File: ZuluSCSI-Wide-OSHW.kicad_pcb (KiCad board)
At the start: 4 copper layers, 100 x 93.5 mm, 170 parts, among them J1 USB_DATA, J2 TF003, J3 Conn_01x02, J4 MnL, J5 HD68, J6 Conn_01x05, J7 Conn_01x04, J8 Conn_01x02, Q1 AO3401A, Q10 AO3401A, Q11 AO3401A, Q12 AO3401A, Q13 AO3401A, Q14 AO3401A, Q15 AO3401A, Q16 AO3401A, Q17 AO3401A, Q18 AO3401A, Q19 AO3401A, Q2 AO3401A, Q20 AO3401A, Q21 AO3401A, Q22 AO3401A, Q23 AO3401A, Q24 AO3401A, Q25 AO3401A, Q26 AO3401A, Q27 AO3401A, Q3 AO3401A, Q4 AO3401A, Q5 AO3401A, Q6 AO3401A, Q7 AO3401A, Q8 AO3401A, Q9 AO3401A, SW1 SW_DIP_x03, SW2 SW_EJECT, SW3 SW_BOOT, U1 RP2350_80QFN, U10 W25Q128JVS, U11 74LVT245, U2 74LVT245, U3 74LVT245, U4 74LVT245, U5 74LVT125, U6 74LVT125, U7 AZ1117-2.85, U8 AP62250WU, U9 USB TVS, Y1 12MHz

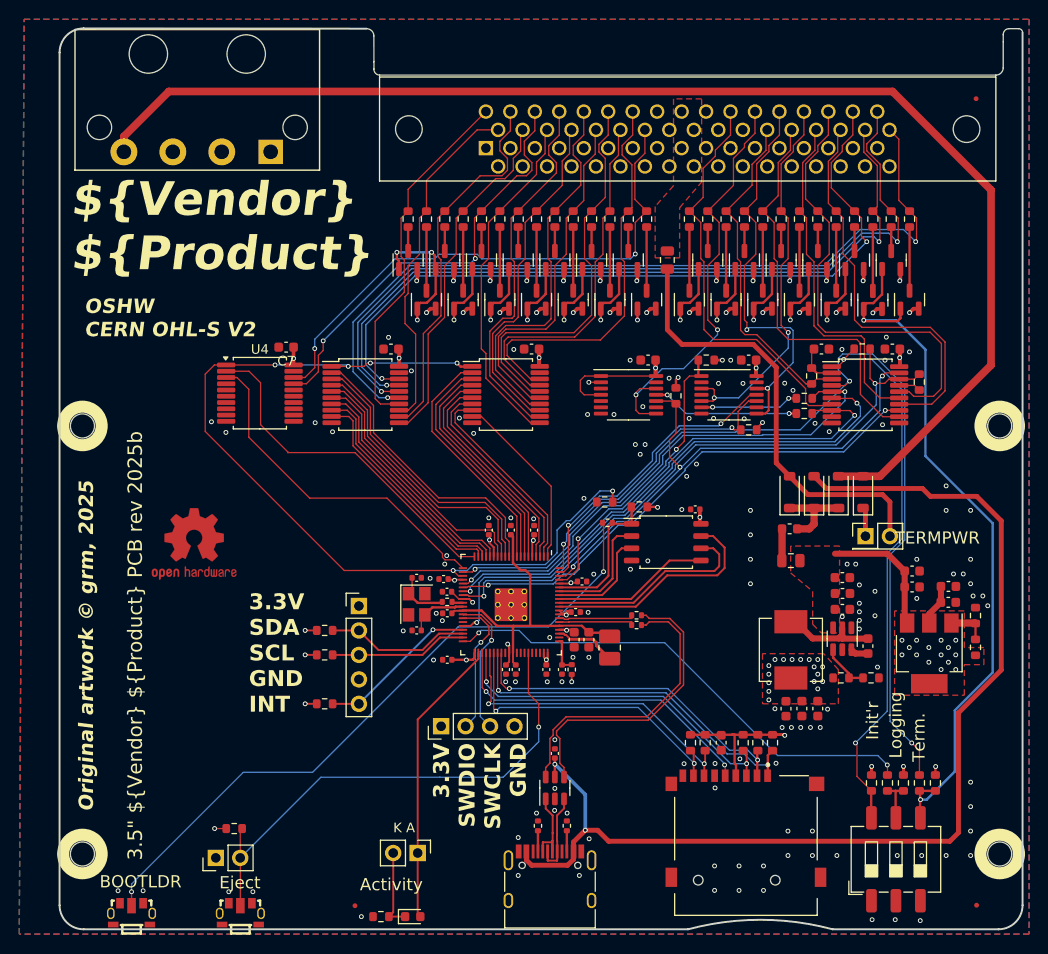
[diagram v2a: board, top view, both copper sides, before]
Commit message: PCB Update, Layout and DRC passed for rev 2026a
Schematic updated with more features from the ZuluSCSI wide board.
JLCPCB parts orientation and position adjusted.
Silkscreen updated

Features added:
- Pico SWD debug header (3 Pin JST header)
- I2C QWIIC header added (4 pin JST header)
- I2S Header added, compatible with AdaFruit PCM510x I2S DACs
- 4 Pin 0.1" (2.54mm) pitch power header added
- Github Workflow for auto generation of Gerbers, BOM, and Pos files
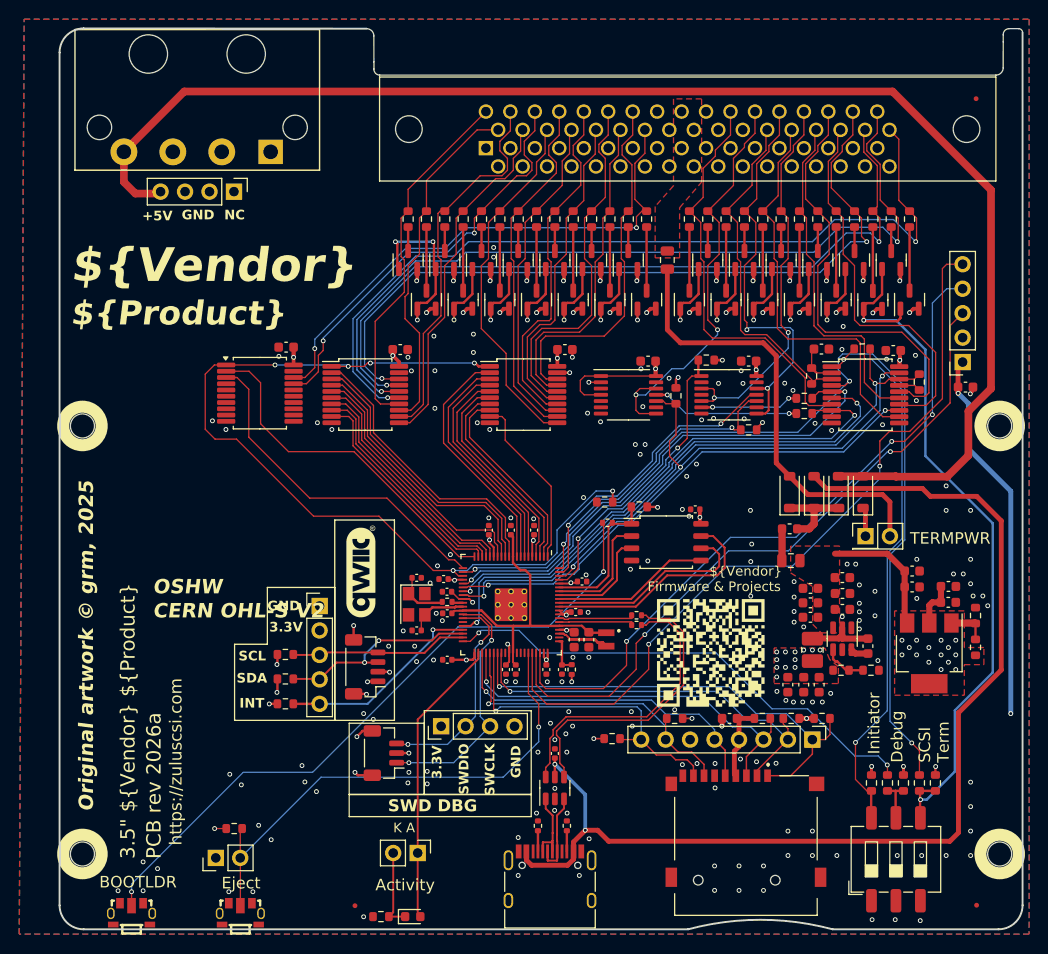
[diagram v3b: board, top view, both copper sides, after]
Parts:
- removed the REF** at (40.8, 96.7)
- added C19: 10uF, Capacitor_SMD:C_0603_1608Metric, F.Cu at (120.9, 80.4)
- added C40: 10uF, Capacitor_SMD:C_0603_1608Metric, F.Cu at (104.8, 101.3)
- added C41: 10uF, Capacitor_SMD:C_0603_1608Metric, F.Cu at (104.8, 104.3)
- added C42: 10uF, Capacitor_SMD:C_0603_1608Metric, F.Cu at (104.8, 102.8)
- added J10: I2S, ZuluSCSI-Wide-OSHW:PCM510x_1x05_P2.54mm_Vertical, F.Cu at (120.6, 77.8)
- added J11: SD_HEADER, Connector_PinHeader_2.54mm:PinHeader_1x08_P2.54mm_Vertical, F.Cu at (105.0, 117.0)
- added J303: QWIIC, Connector_JST:JST_SH_BM04B-SRSS-TB_1x04-1MP_P1.00mm_Vertical, F.Cu at (58.6, 109.4)
- added J311: PICO_DBG, Connector_JST:JST_SH_BM03B-SRSS-TB_1x03-1MP_P1.00mm_Vertical, F.Cu at (60.5, 118.4)
- added J9: PHeader, Connector_PinHeader_2.54mm:PinHeader_1x04_P2.54mm_Vertical, F.Cu at (44.9, 60.1)
- added REF**: OSHW-Logo2_14.6x12mm_Copper, Symbol:OSHW-Logo2_14.6x12mm_Copper, F.Cu at (43.4, 94.1)
- L2: footprint Inductor_SMD:L_Vishay_IHLP-2525 -> Inductor_SMD:L_1008_2520Metric_Pad1.43x2.20mm_HandSolder
- L3: value 3.3uH -> 3.3u; footprint Inductor_SMD:L_1008_2520Metric_Pad1.43x2.20mm_HandSolder -> ZuluSCSI-Wide-OSHW:L_pol_2016
- SW2: value SW_EJECT -> SW_PUSH
- SW3: value SW_BOOT -> SW_PUSH
- moved R7 8.15 mm to (84.2, 116.9), turned to 180 degrees
- moved R1 5.73 mm to (106.0, 114.8), turned to 180 degrees
- moved R51 4.78 mm to (50.3, 110.7)
- moved R15 4.78 mm to (50.3, 108.2)
- moved R2 4.28 mm to (102.8, 114.8), turned to 0 degrees
- moved C16 4.25 mm to (105.7, 111.3)
- moved J6 4.08 mm to (53.8, 103.1)
- moved R52 4.08 mm to (50.3, 113.3)
- moved R5 4.05 mm to (90.7, 114.8), turned to 0 degrees
- moved C4 3.46 mm to (79.3, 76.5), turned to 0 degrees
- moved R3 3.21 mm to (99.8, 114.8), turned to 180 degrees
- moved C12 2.88 mm to (104.1, 111.3)
- moved C13 2.88 mm to (102.4, 111.3)
- moved C1 2.67 mm to (96.4, 114.8), turned to 180 degrees
- moved L2 2.23 mm to (105.0, 107.7)
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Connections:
- J6 pad 1: +3V3 -> GND
- J6 pad 2: /I²C_SDA -> +3V3
- J6 pad 4: GND -> /I²C_SDA
- R15 pad 1: /I²C_SDA -> /I²C_SCL
- R51 pad 1: /I²C_SCL -> /I²C_SDA
- U1 pad 56: unconnected-(U1-GPIO45_ADC5-Pad56) -> /I2S_CK
- U1 pad 57: unconnected-(U1-GPIO46_ADC6-Pad57) -> /I2S_WS
- U1 pad 58: unconnected-(U1-GPIO47_ADC7-Pad58) -> /I2S_SD
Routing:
- net /I2S_CK: track 0.00 -> 79.8 mm, vias 0 -> 2
- net /I2S_SD: track 0.00 -> 72.7 mm, vias 0 -> 3
- net /I2S_WS: track 0.00 -> 70.9 mm, vias 0 -> 2
- net +3V3: track 50.1 -> 86.2 mm
- net GND: track 1.25 -> 14.0 mm, vias 132 -> 185
- net /SWCLK: track 14.9 -> 26.1 mm, vias 1 -> 2
- net /SDIO_D2: track 37.9 -> 49.2 mm, vias 2 -> 1
- net /5V_IN: track 136.6 -> 147.4 mm
- net /SWD: track 14.4 -> 22.4 mm, vias 1 -> 2
- net /SDIO_D3: track 35.6 -> 42.8 mm, vias 2 -> 1
- net /I²C_SDA: track 15.1 -> 21.5 mm, vias 0 -> 2
- net /SDIO_CMD: track 36.5 -> 41.5 mm, vias 2 -> 1
- net /I²C_INT: track 16.7 -> 21.3 mm
- net /I²C_SCL: track 14.3 -> 18.4 mm
- net /~{SCSI_SD7}: track 41.6 -> 37.8 mm
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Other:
- board text added: "${Product}"
- board text added: "${Vendor}"
- board text added: "+5V"
- board text added: "3.3V"
- board text added: "3.5{dblquote} ${Vendor} ${Product}"
- board text added: "3V3"
- board text added: "CERN OHL-S V2"
- board text added: "CLK"
- board text added: "CMD"
- board text added: "D0"
- board text added: "D1"
- board text added: "D2"
- board text added: "D3"
- board text added: "Debug"
- board text added: "Firmware & Projects"
- board text added: "GND"
- board text added: "INT"
- board text added: "Initiator"
- board text added: "NC"
- board text added: "OSHW"
- board text added: "PCB rev ${REVISION}"
- board text added: "SCL"
- board text added: "SCSI Term"
- board text added: "SDA"
- board text added: "SDIO"
- board text added: "SWCLK"
- board text added: "SWD DBG"
- board text added: "SWDIO"
- board text added: "ZuluSCSI Firmware & Projects"
- board text added: "https://zuluscsi.com"
- board text removed: "${Vendor} ${Product}"
- board text removed: "3.3V SDA SCL GND INT"
- board text removed: "3.3V SWDIO SWCLK GND"
- board text removed: "3.5{dblquote} ${Vendor} ${Product} PCB rev ${REVISION}"
- board text removed: "Init'r"
- board text removed: "Logging"
- board text removed: "OSHW CERN OHL-S V2"
- board text removed: "Term."
